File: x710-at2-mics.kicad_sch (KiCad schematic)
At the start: 36 parts, among them U1 EZX710AT2_S_LMR5, U2 74LVC1G07_SOT-753

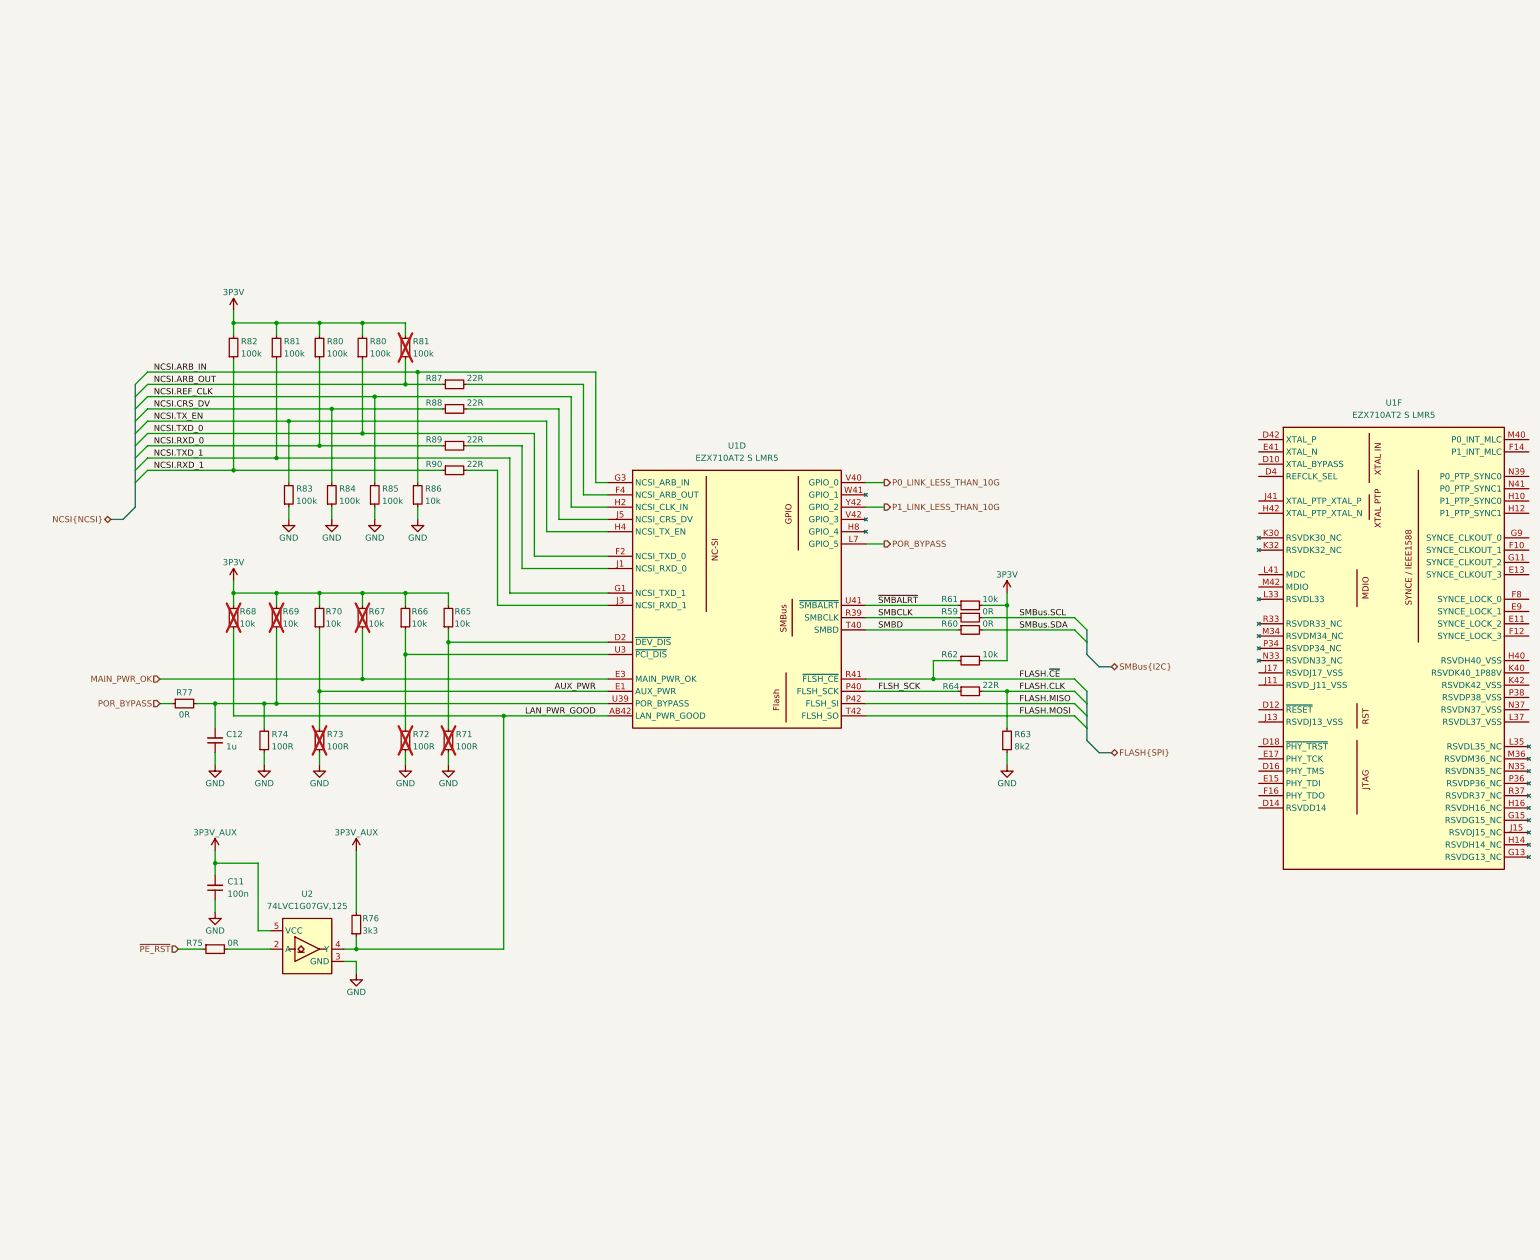
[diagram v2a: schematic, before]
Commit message: [#80813] Add misc, improve schematic readability
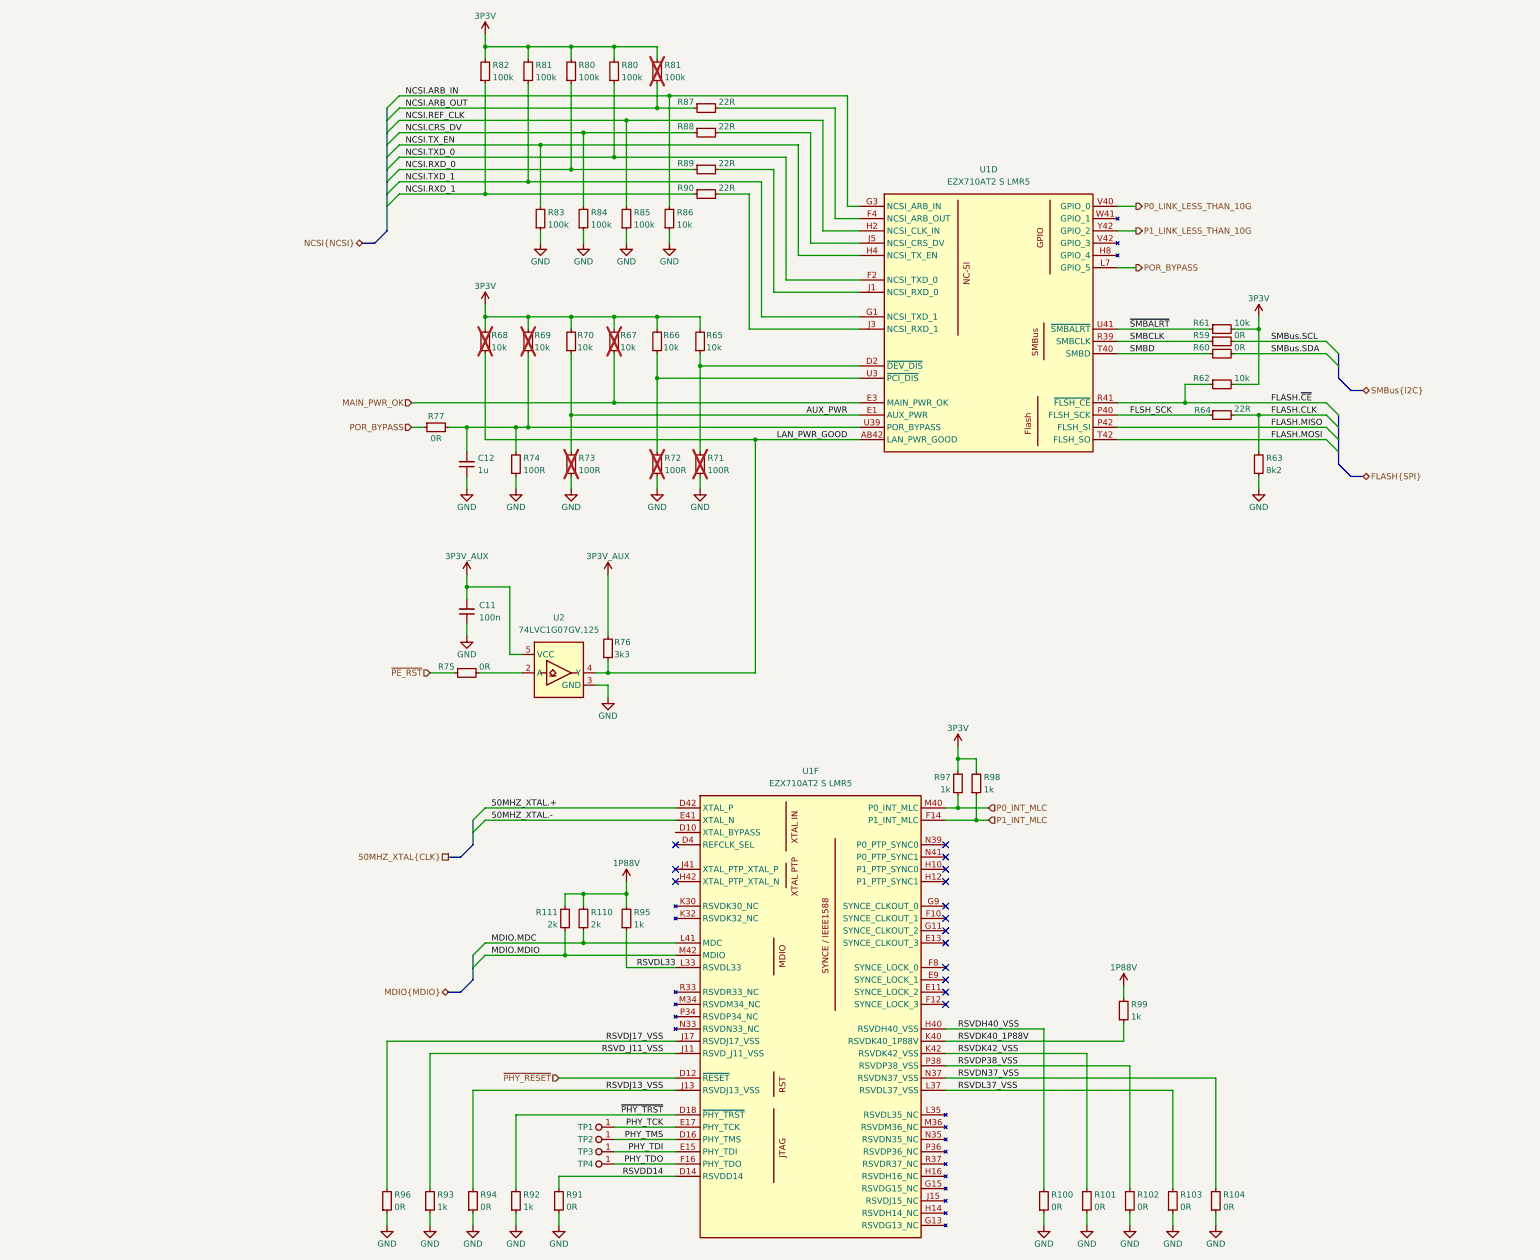
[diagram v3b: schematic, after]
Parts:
- added R100, R101, R102, R103, R104, R91, R94, R96: R_0R_0402, antmicro-footprints:R_0402_1005Metric, symbol antmicroResistors0402:R_0R_0402
- added R110, R111: R_2k_0402, antmicro-footprints:R_0402_1005Metric, symbol antmicroResistors0402:R_2k_0402
- added R92, R93, R95, R97, R98, R99: R_1k_0402, antmicro-footprints:R_0402_1005Metric, symbol antmicroResistors0402:R_1k_0402
- added TP1, TP2, TP3, TP4: TP_0.75mm_SMD, antmicro-footprints:TP_SMD_0.75mm, symbol antmicroTestPoints:TP_0.75mm_SMD
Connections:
- net 3P3V: now also R97.2, R98.2
- net GND: now also R100.1, R101.1, R102.1, R103.1, R104.1, R91.1, R92.1, R93.1, R94.1, R96.1
- net ~{PHY_RESET}: now reaches U1.D12 (~{RESET})
- net RSVDD14: now reaches U1.D14 (RSVDD14)
- net RSVDD14: now also R91.2
- net PHY_TMS: now reaches U1.D16 (PHY_TMS)
- net PHY_TMS: now also TP2.1
- net ~{PHY_TRST}: now reaches U1.D18 (~{PHY_TRST})
- net ~{PHY_TRST}: now also R92.2
- net 50MHZ_XTAL.+: now reaches U1.D42 (XTAL_P)
- net PHY_TDI: now reaches U1.E15 (PHY_TDI)
- net PHY_TDI: now also TP3.1
- net PHY_TCK: now reaches U1.E17 (PHY_TCK)
- net PHY_TCK: now also TP1.1
- net 50MHZ_XTAL.-: now reaches U1.E41 (XTAL_N)
- net P1_INT_MLC: now reaches U1.F14 (P1_INT_MLC)
- net P1_INT_MLC: now also R98.1
- net PHY_TDO: now reaches U1.F16 (PHY_TDO)
- net PHY_TDO: now also TP4.1
- net RSVDH40_VSS: now reaches U1.H40 (RSVDH40_VSS)
- net RSVDH40_VSS: now also R100.2
- net RSVD_J11_VSS: now reaches U1.J11 (RSVD_J11_VSS)
- net RSVD_J11_VSS: now also R93.2
- net RSVDJ13_VSS: now reaches U1.J13 (RSVDJ13_VSS)
- net RSVDJ13_VSS: now also R94.2
- net RSVDJ17_VSS: now reaches U1.J17 (RSVDJ17_VSS)
- net RSVDJ17_VSS: now also R96.2
- net RSVDK40_1P88V: now reaches U1.K40 (RSVDK40_1P88V)
- net RSVDK40_1P88V: now also R99.1
- net RSVDK42_VSS: now reaches U1.K42 (RSVDK42_VSS)
- net RSVDK42_VSS: now also R101.2
- net RSVDL33: now reaches U1.L33 (RSVDL33)
- net RSVDL33: now also R95.1
- net RSVDL37_VSS: now reaches U1.L37 (RSVDL37_VSS)
- net RSVDL37_VSS: now also R103.2
- net MDIO.MDC: now reaches U1.L41 (MDC)
- net MDIO.MDC: now also R110.1
- net P0_INT_MLC: now reaches U1.M40 (P0_INT_MLC)
- net P0_INT_MLC: now also R97.1
- net MDIO.MDIO: now reaches U1.M42 (MDIO)
- net MDIO.MDIO: now also R111.1
- net RSVDN37_VSS: now reaches U1.N37 (RSVDN37_VSS)
- net RSVDN37_VSS: now also R104.2
- net RSVDP38_VSS: now reaches U1.P38 (RSVDP38_VSS)
- net RSVDP38_VSS: now also R102.2
- new net 1P88V: R110.2, R111.2, R95.2, R99.2
- no-connect marks 0 -> 15
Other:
- moved on the sheet: C11, C12, R59, R60, R61, R62, R63, R64, R65, R66, R67, R68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

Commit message: [#80813] Change RJ45 connectors, reannotate schematics
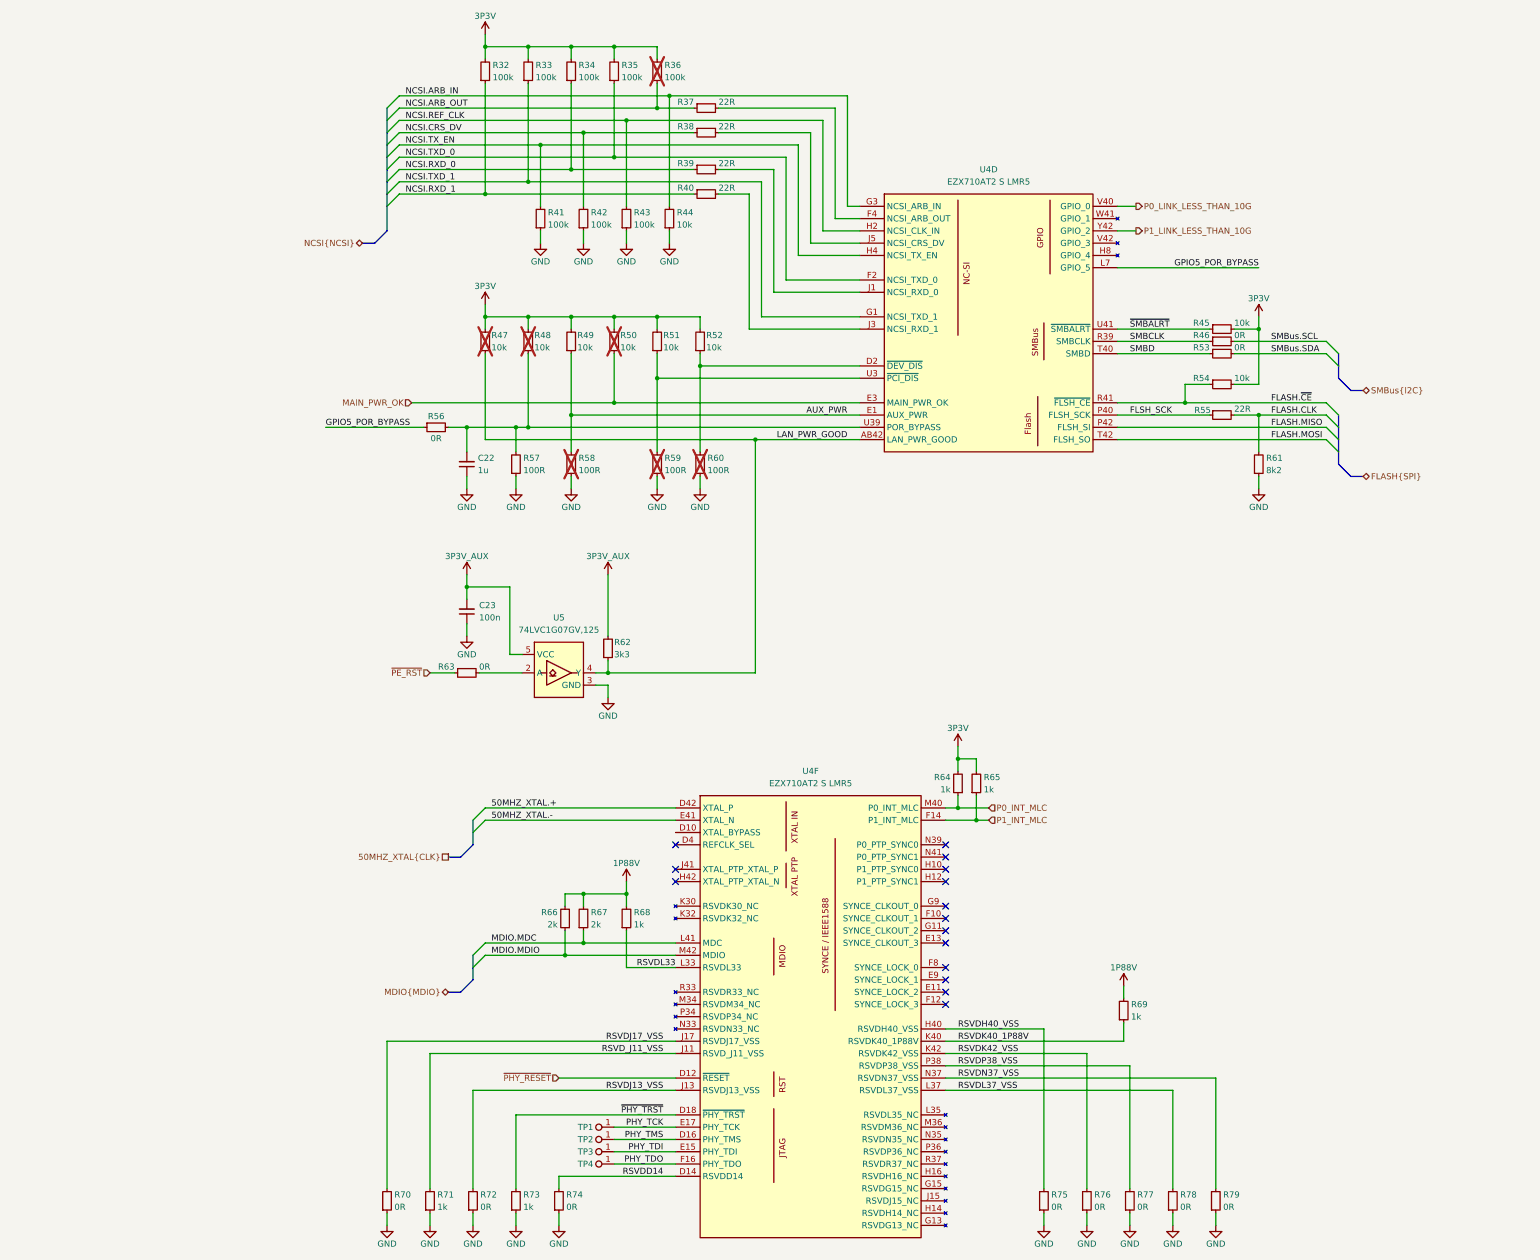
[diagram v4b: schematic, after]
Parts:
- renumbered C12 to C22, C11 to C23, R82 to R32, R81 to R33, R80 to R34, R80 to R35, R81 to R36, R87 to R37, R88 to R38, R89 to R39, R90 to R40, R83 to R41, R84 to R42, R85 to R43, R86 to R44, R61 to R45, R59 to R46, R68 to R47, R69 to R48, R70 to R49, R67 to R50, R66 to R51, R65 to R52, R60 to R53, R62 to R54, R64 to R55, R77 to R56, R74 to R57, R73 to R58, R72 to R59, R71 to R60, R63 to R61, R76 to R62, R75 to R63, R97 to R64, R98 to R65, R111 to R66, R110 to R67, R95 to R68, R99 to R69, R96 to R70, R93 to R71, R94 to R72, R92 to R73, R91 to R74, R100 to R75, R101 to R76, R102 to R77, R103 to R78, R104 to R79, U1 to U4, U2 to U5
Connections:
- net POR_BYPASS renamed GPIO5_POR_BYPASS

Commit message: [#80813] Improve schematic readability, add debug connectors and missing resistors
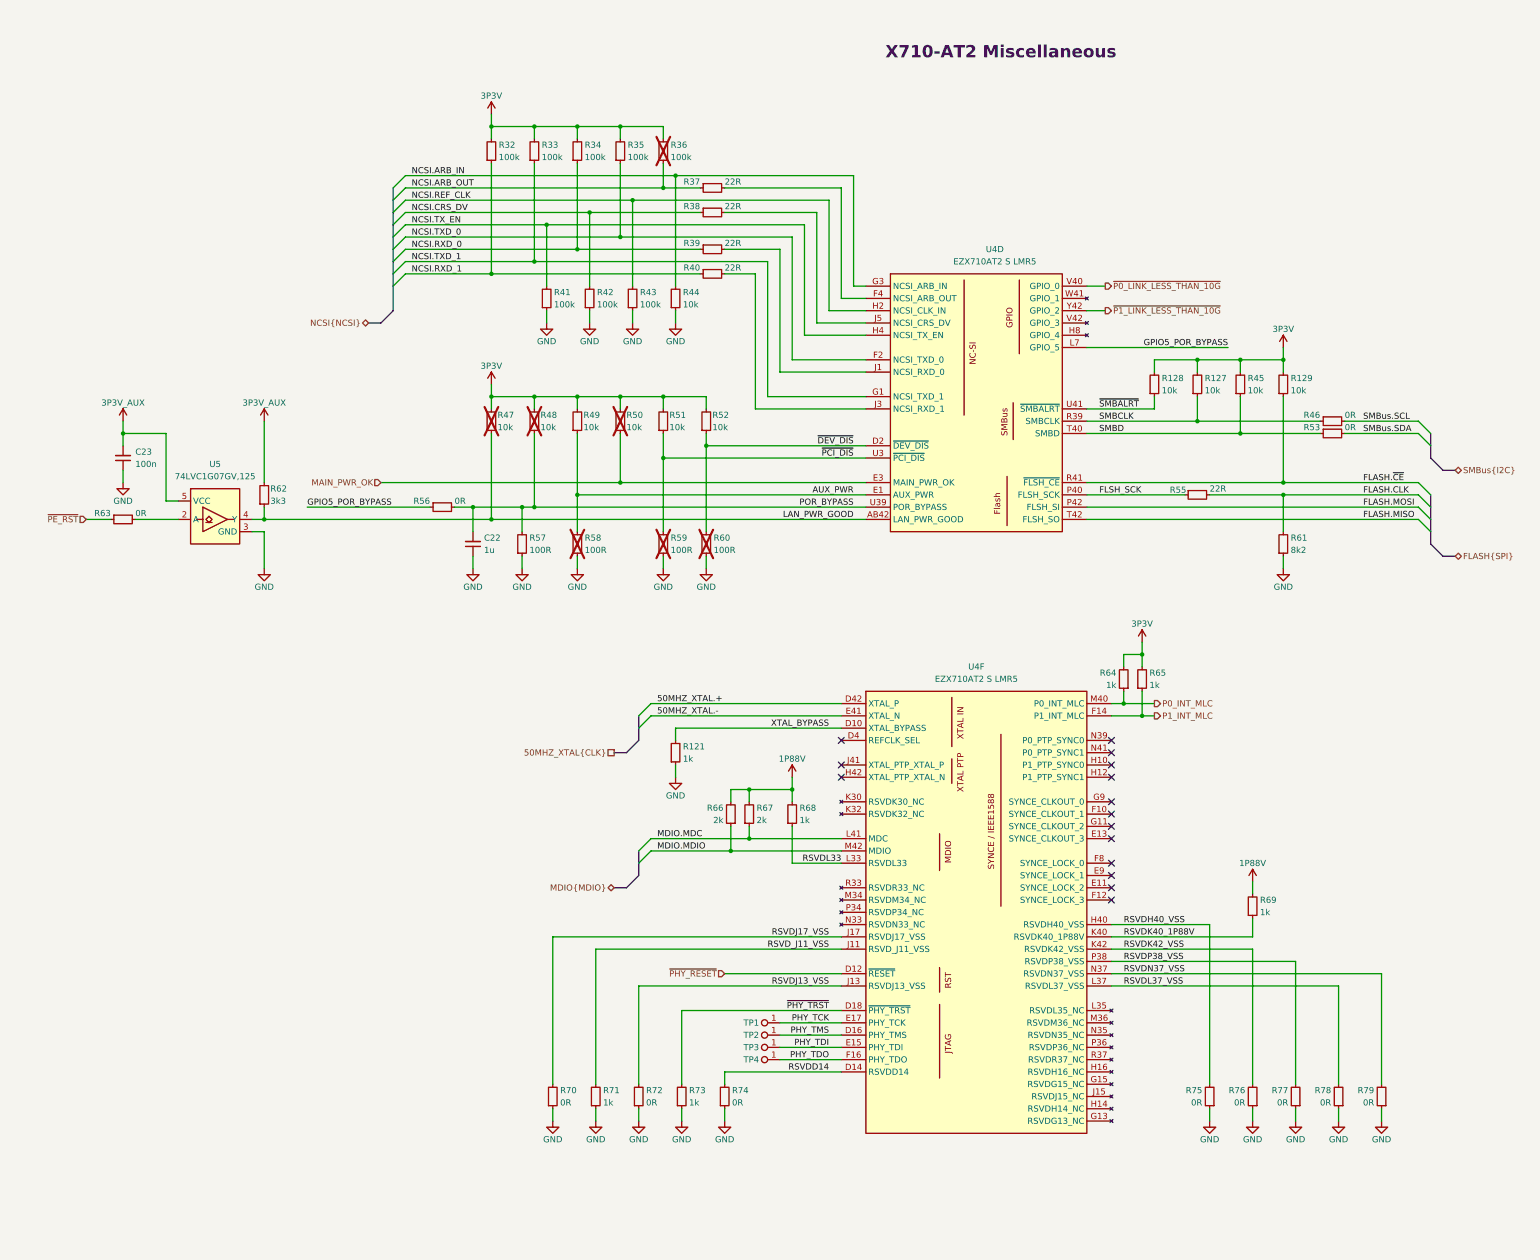
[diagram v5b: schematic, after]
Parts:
- removed R54: R_10k_0402, antmicro-footprints:R_0402_1005Metric, symbol antmicroResistors0402:R_10k_0402
- added R121: R_1k_0402, antmicro-footprints:R_0402_1005Metric, symbol antmicroResistors0402:R_1k_0402
- added R127, R128, R129: R_10k_0402, antmicro-footprints:R_0402_1005Metric, symbol antmicroResistors0402:R_10k_0402
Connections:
- net 3P3V: now also R127.2, R128.2, R129.2
- net FLASH.MISO: now also U4.T42 (FLSH_SO); no longer U4.P42 (FLSH_SI)
- net FLASH.MOSI: now also U4.P42 (FLSH_SI); no longer U4.T42 (FLSH_SO)
- net FLASH.~{CE}: now also R129.1
- net GND: now also R121.1
- net SMBCLK: now also R127.1
- net SMBD: now also R45.1
- net ~{SMBALRT}: now also R128.1; no longer R45.1
- net ~{PCI_DIS}: now reaches R51.1, R59.2, U4.U3 (~{PCI_DIS})
- net ~{DEV_DIS}: now reaches R52.1, R60.2, U4.D2 (~{DEV_DIS})
- net POR_BYPASS: now reaches C22.2, R48.1, R56.2, R57.2, U4.U39 (POR_BYPASS)
- net XTAL_BYPASS: now reaches U4.D10 (XTAL_BYPASS)
- net XTAL_BYPASS: now also R121.2
- net P0_LINK_LESS_THAN_10G renamed ~{P0_LINK_LESS_THAN_10G}
- net P1_LINK_LESS_THAN_10G renamed ~{P1_LINK_LESS_THAN_10G}
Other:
- note added: "X710-AT2 Miscellaneous"
- moved on the sheet: C22, C23, R32, R33, R34, R35, R36, R37, R38, R39, R40, R41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
